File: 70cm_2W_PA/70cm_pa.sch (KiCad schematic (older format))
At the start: 43 parts, among them J1 Conn_Coaxial, J2 Conn_Coaxial, J3 Conn_01x02, J4 Conn_01x02, U1 M68710L, U2 MIC5205YM5, U3 SN74LV1T08, U4 LM75B

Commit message: Schematic fixes and a bit of layout
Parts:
- removed J4: Conn_01x02, symbol Connector_Generic:Conn_01x02
- removed U3: SN74LV1T08, symbol 74xGxx:74LVC1G00
- added C10, C9: 100n, Capacitor_SMD:C_0805_2012Metric, symbol Device:C
- added J4: ~, 70cm_pa:Pigtail, symbol Connector:Conn_Coaxial
- added R11: 1, Resistor_SMD:R_0805_2012Metric, symbol Device:R
- added R15: 0, Resistor_SMD:R_0805_2012Metric, symbol Device:R
- added R16: 100k, Resistor_SMD:R_0805_2012Metric, symbol Device:R
- added U3: SN74LV1T08, Package_TO_SOT_SMD:SOT-23-5, symbol 74xGxx:74LVC1G08
- J1, J2: value Conn_Coaxial -> ~; footprint Connector_Coaxial:SMA_Amphenol_132134-10_Vertical -> 70cm_pa:Pigtail
- J3: footprint (none) -> 70cm_pa:DC_Pad
- R18: renamed from R17; value 1k -> 0
- TH1: footprint (none) -> Resistor_SMD:R_0805_2012Metric
- renumbered R11 to R12, R12 to R13, R13 to R14, R14 to R17, R18 to R19, R15 to R20, R16 to R21, R19 to R22
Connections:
- net labels added: LM_VDD, NTC
- wire segments 73 -> 83
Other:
- note added: "Place either pull-up\nor pull-down in EN"
- moved on the sheet: C7, R10, R12, R13, R14, R17, R20, R21, R22, R9, TH1, U4

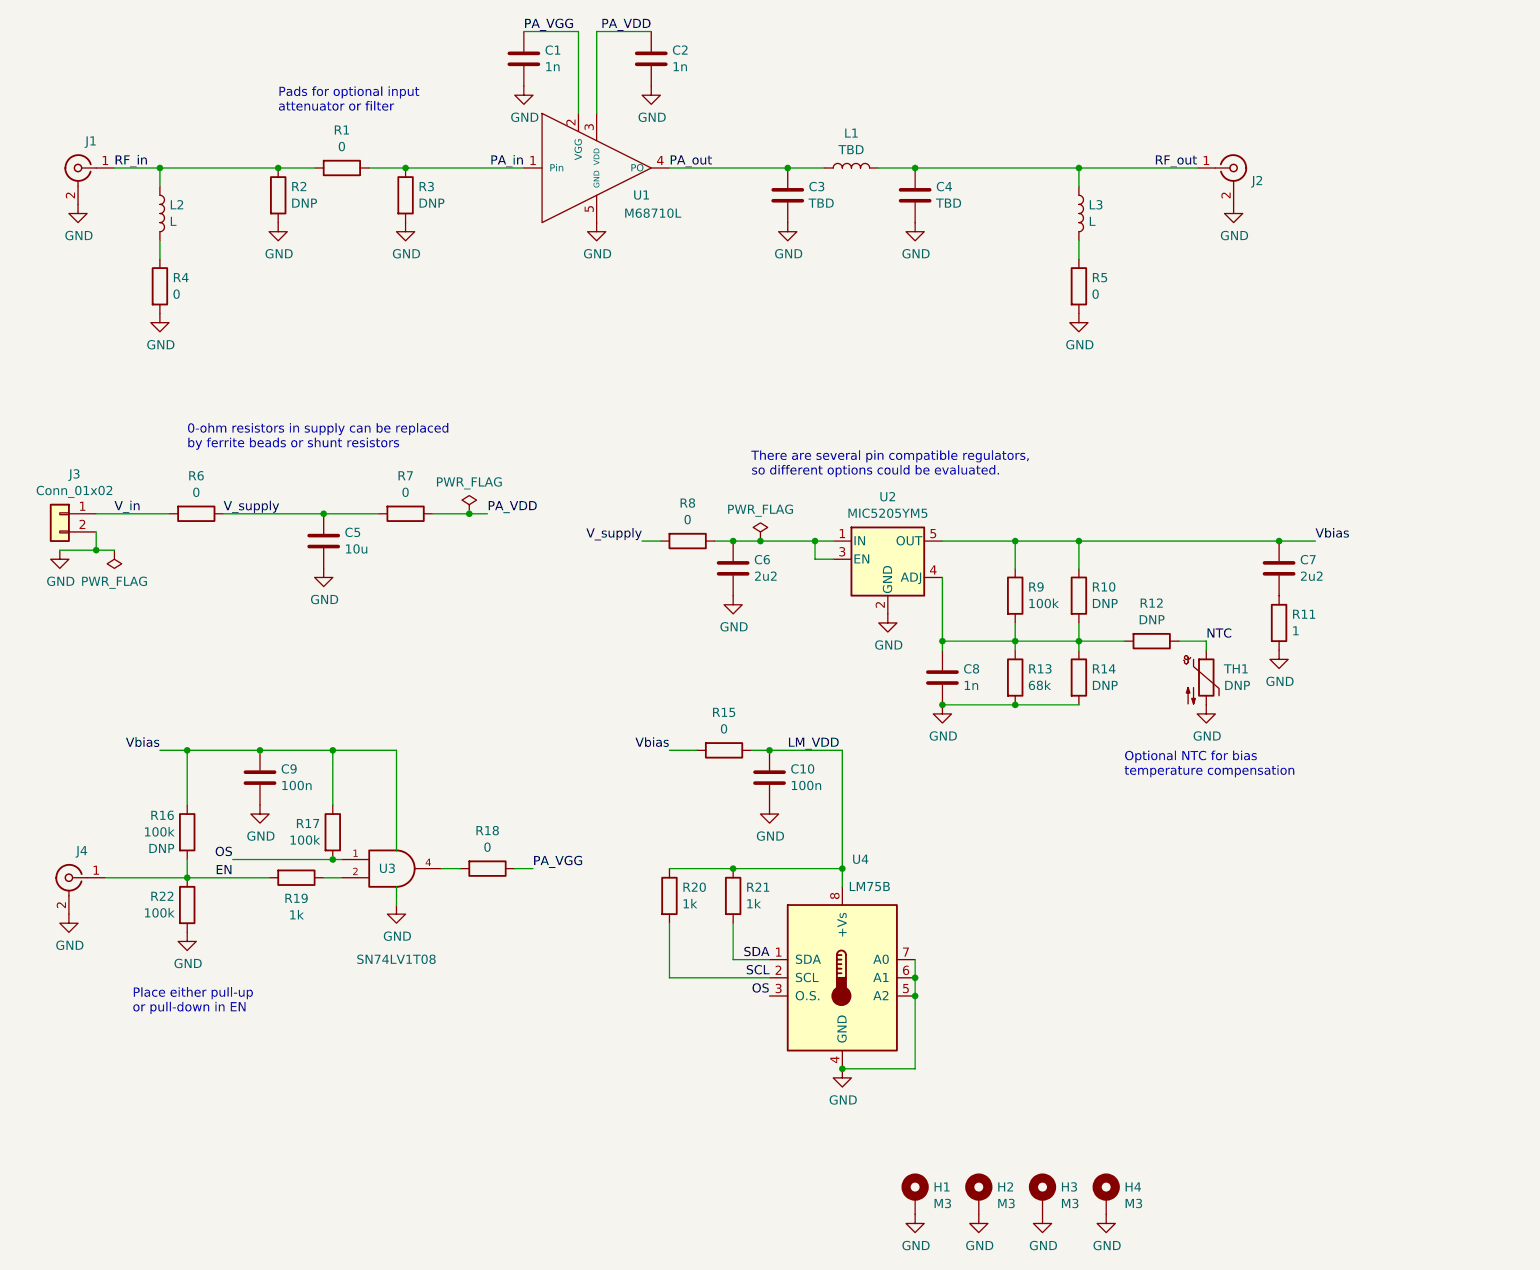
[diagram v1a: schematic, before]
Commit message: Most components connected in layout (M68710L)
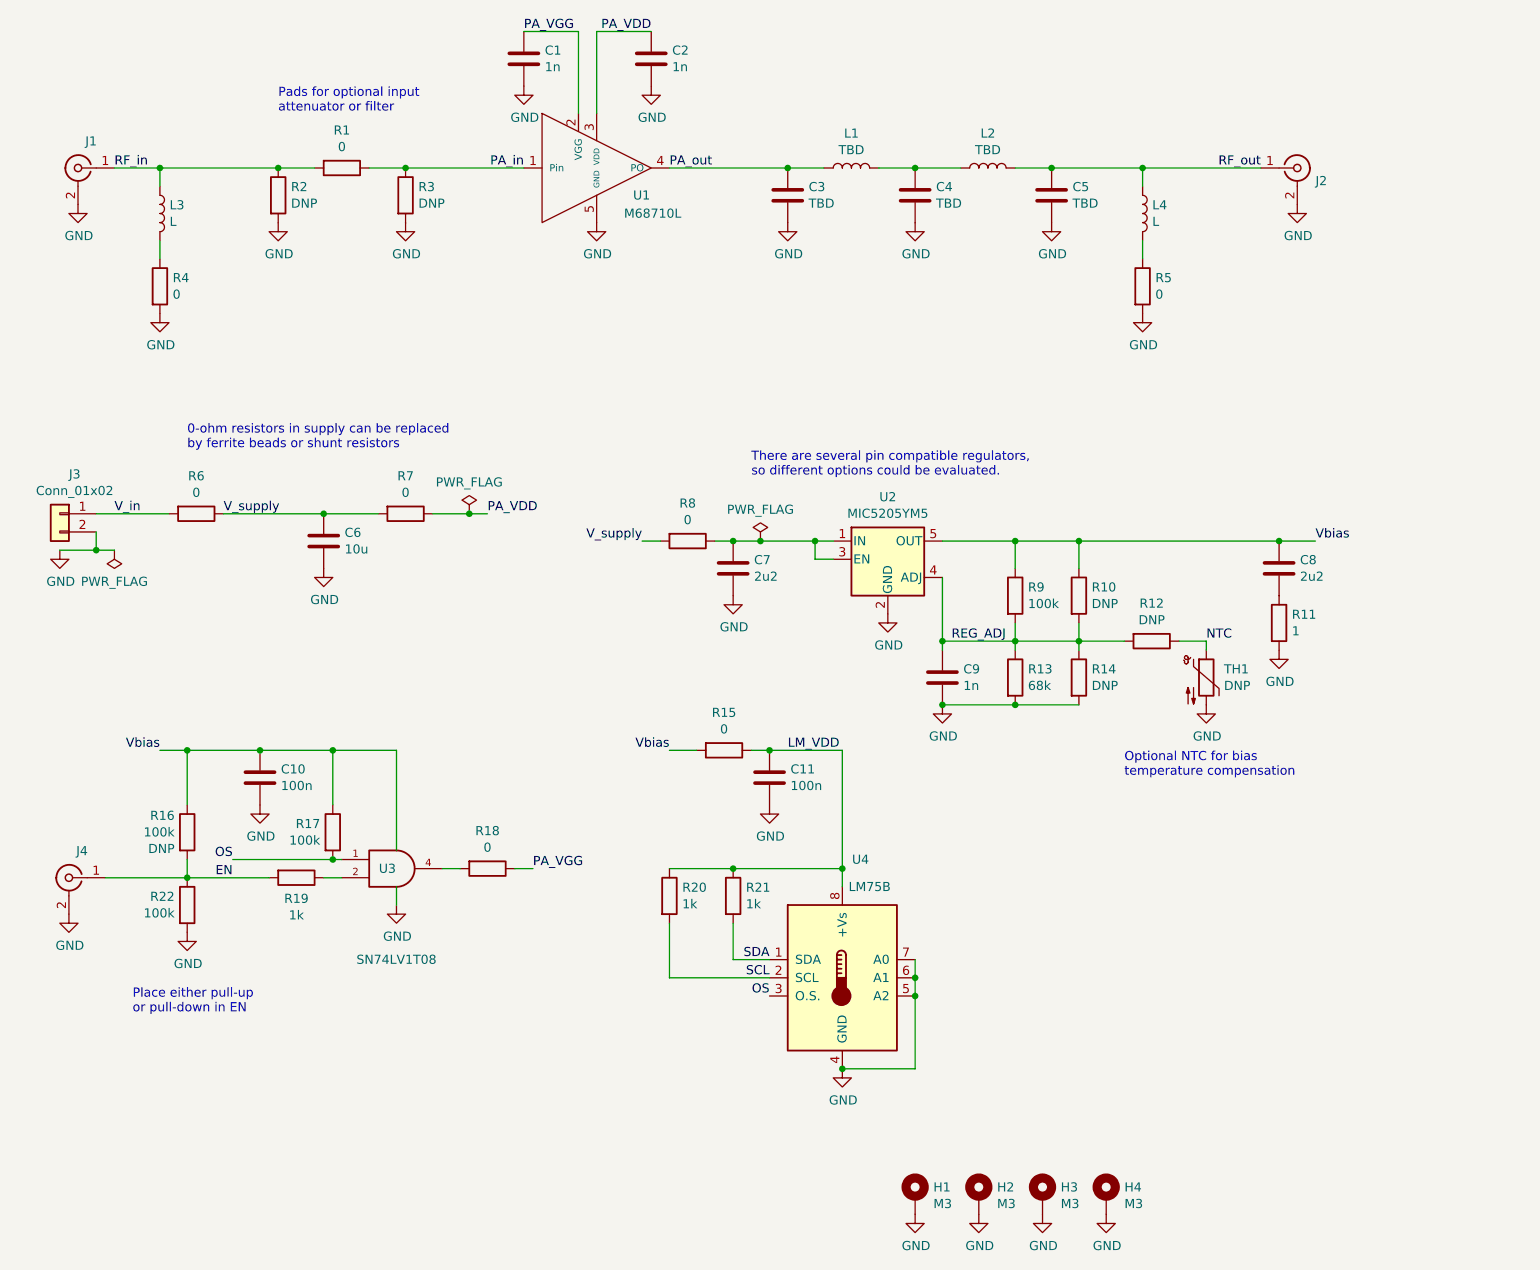
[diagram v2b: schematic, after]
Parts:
- added C5: TBD, Capacitor_SMD:C_0805_2012Metric, symbol Device:C
- added L2: TBD, Inductor_SMD:L_0805_2012Metric, symbol Device:L
- renumbered C9 to C10, C10 to C11, C5 to C6, C6 to C7, C7 to C8, C8 to C9, L2 to L3, L3 to L4
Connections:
- net GND: now also C5.2
- net RF_out: now also C5.1, L2.2; no longer C4.1, L1.2
- net REG_ADJ: now reaches C9.1, R10.2, R12.2, R13.1, R14.1, R9.2, U2.4 (ADJ)
- new net: C4.1, L1.2, L2.1
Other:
- moved on the sheet: J2, L4, R5

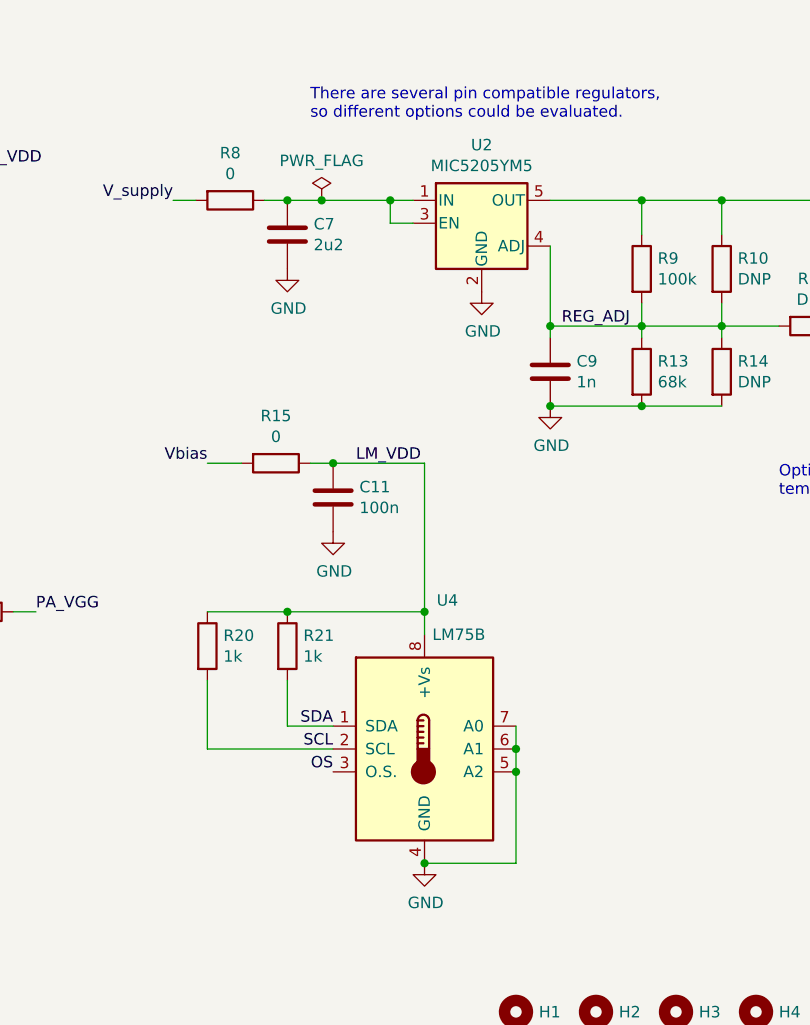
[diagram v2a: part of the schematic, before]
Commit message: M68710L: rearrange layout a bit
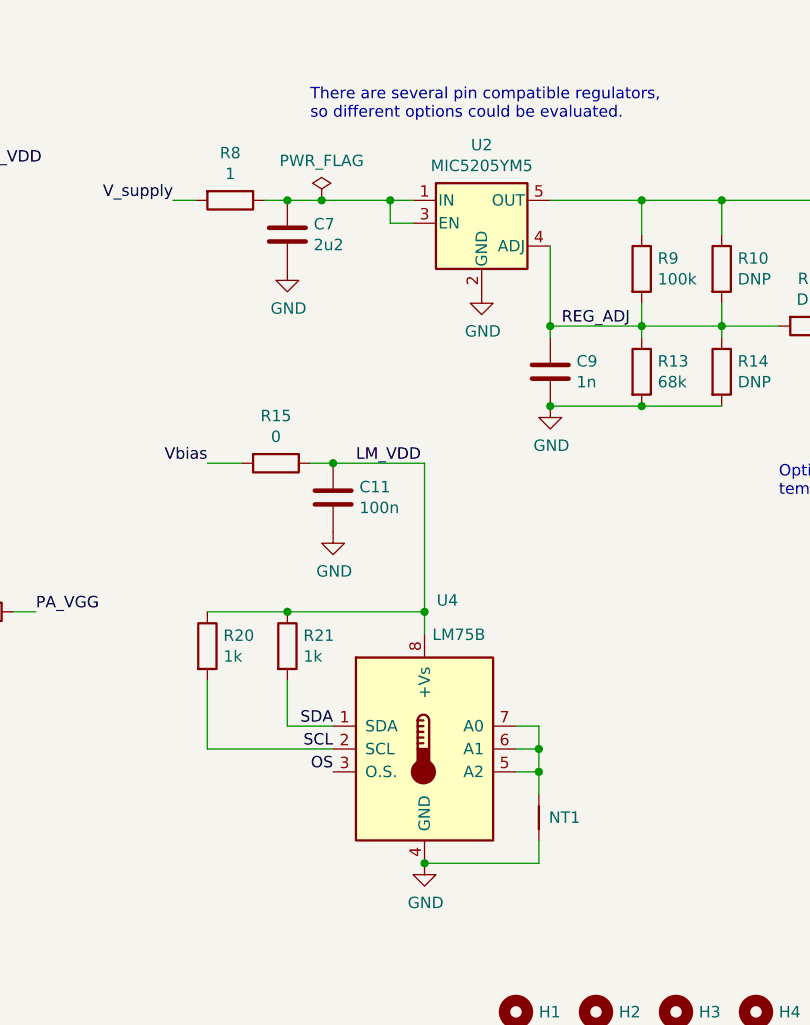
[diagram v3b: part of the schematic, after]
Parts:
- added NT1: ~, NetTie:NetTie-2_SMD_Pad0.5mm, symbol Device:Net-Tie_2
- R8: value 0 -> 1
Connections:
- net GND: now also NT1.2; no longer U4.5 (A2), U4.6 (A1), U4.7 (A0)
- new net: NT1.1, U4.5 (A2), U4.6 (A1), U4.7 (A0)
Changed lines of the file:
@@
 Text Label 4100 950  2    50   ~ 0
 PA_VDD
-Wire Wire Line
-	5550 6050 5550 6150
-Wire Wire Line
-	5550 6650 5150 6650
-Connection ~ 5550 6150
-Wire Wire Line
-	5550 6150 5550 6250
-Connection ~ 5550 6250
-Wire Wire Line
-	5550 6250 5550 6650
 Connection ~ 5150 6650
 Text Label 4750 6050 2    50   ~ 0
@@
 P 4300 3750
 F 0 "R8" V 4093 3750 50  0000 C CNN
-F 1 "0" V 4184 3750 50  0000 C CNN
+F 1 "1" V 4184 3750 50  0000 C CNN
 F 2 "Resistor_SMD:R_0805_2012Metric" V 4230 3750 50  0001 C CNN
 F 3 "~" H 4300 3750 50  0001 C CNN
@@
 Text Label 5750 4300 0    50   ~ 0
 REG_ADJ
+$Comp
+L Device:Net-Tie_2 NT1
+U 1 1 5DB79A0B
+P 5650 6450
+F 0 "NT1" V 5650 6494 50  0000 L CNN
+F 1 "~" V 5695 6494 50  0000 L CNN
+F 2 "NetTie:NetTie-2_SMD_Pad0.5mm" H 5650 6450 50  0001 C CNN
+F 3 "~" H 5650 6450 50  0001 C CNN
+	1    5650 6450
+	0    1    1    0
+$EndComp
+Wire Wire Line
+	5650 6350 5650 6250
+Wire Wire Line
+	5650 6050 5550 6050
+Wire Wire Line
+	5550 6150 5650 6150
+Connection ~ 5650 6150
+Wire Wire Line
+	5650 6150 5650 6050
+Wire Wire Line
+	5550 6250 5650 6250
+Connection ~ 5650 6250
+Wire Wire Line
+	5650 6250 5650 6150
+Wire Wire Line
+	5650 6550 5650 6650
+Wire Wire Line
+	5150 6650 5650 6650
 $EndSCHEMATC
